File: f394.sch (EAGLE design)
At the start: 4 parts

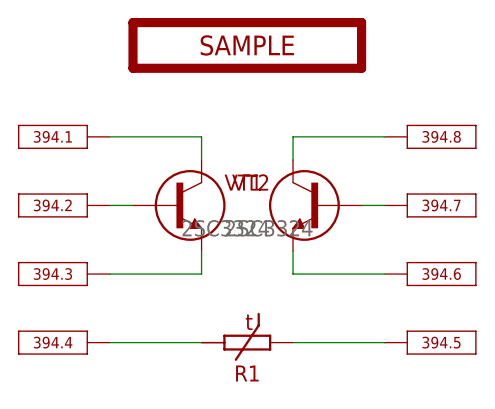
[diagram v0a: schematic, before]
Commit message: Update F394 to use PMP4201Y
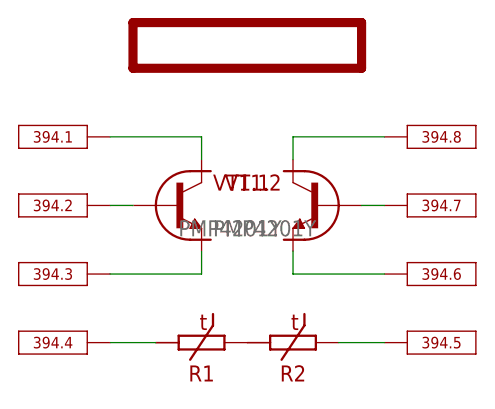
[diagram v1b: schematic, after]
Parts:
- removed VT2: 2SC3324, transistors-npn:2SC3324
- added R2: (no value), resistors:ERA-V33J102V
- 394: value SAMPLE -> (none)
- VT1: value 2SC3324 -> PMP4201Y; device transistors-npn:2SC3324 -> transistors-npn:PMP4201Y
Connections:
- removed net N$2: 394.2.PIN, VT1.B
- removed net N$5: 394.7.PIN, VT2.B
- removed net N$9 (its old number): 394.5.PIN, R1.E
- new net B1: 394.2.PIN, VT1.1.B
- new net B2: 394.7.PIN, VT1.2.B
- new net N$10: 394.5.PIN, R2.E
- new net N$7: R1.E, R2.A
- net N$1: now also VT1.1.C; no longer VT1.C
- net N$3: now also VT1.2.E; no longer VT2.E
- net N$4: now also VT1.2.C; no longer VT2.C
- net N$6: now also VT1.1.E; no longer VT1.E
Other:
- moved on the sheet: R1
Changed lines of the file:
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@@
 <?xml version="1.0" encoding="utf-8"?>
 <!DOCTYPE eagle SYSTEM "eagle.dtd">
-<eagle version="7.5.0">
+<eagle version="7.5.1">
 <drawing>
 <settings>
@@
 </classes>
 <parts>
-<part name="394" library="module-footprints" deviceset="DIP8" device="" value="SAMPLE"/>
-<part name="VT1" library="transistors-npn" deviceset="?" device="2SC3324"/>
-<part name="VT2" library="transistors-npn" deviceset="?" device="2SC3324"/>
+<part name="394" library="module-footprints" deviceset="DIP8" device=""/>
 <part name="R1" library="resistors" deviceset="ERA-?33J*V" device="V" technology="102"/>
+<part name="R2" library="resistors" deviceset="ERA-?33J*V" device="V" technology="102"/>
+<part name="VT1" library="transistors-npn" deviceset="PMP4201Y" device=""/>
 </parts>
 <sheets>
@@
 <instance part="394" gate=".5" x="76.2" y="50.8" rot="R180"/>
 <instance part="394" gate="G$1" x="58.42" y="83.82" rot="R180"/>
-<instance part="VT1" gate="G$1" x="50.8" y="66.04"/>
-<instance part="VT2" gate="G$1" x="66.04" y="66.04" rot="MR0"/>
-<instance part="R1" gate="G$1" x="58.42" y="50.8"/>
+<instance part="R1" gate="G$1" x="53.34" y="50.8"/>
+<instance part="R2" gate="G$1" x="63.5" y="50.8"/>
+<instance part="VT1" gate=".1" x="53.34" y="66.04"/>
+<instance part="VT1" gate=".2" x="63.5" y="66.04" rot="MR0"/>
 </instances>
 <busses>
@@
 <segment>
 <pinref part="394" gate=".1" pin="PIN"/>
-<pinref part="VT1" gate="G$1" pin="C"/>
 <wire x1="43.18" y1="73.66" x2="53.34" y2="73.66" width="0.1524" layer="91"/>
 <wire x1="53.34" y1="73.66" x2="53.34" y2="71.12" width="0.1524" layer="91"/>
-</segment>
-</net>
-<net name="N$2" class="0">
-<segment>
-<pinref part="VT1" gate="G$1" pin="B"/>
+<pinref part="VT1" gate=".1" pin="C"/>
+</segment>
+</net>
+<net name="B1" class="0">
+<segment>
 <pinref part="394" gate=".2" pin="PIN"/>
 <wire x1="45.72" y1="66.04" x2="43.18" y2="66.04" width="0.1524" layer="91"/>
+<pinref part="VT1" gate=".1" pin="B"/>
 </segment>
 </net>
@@
 <segment>
 <pinref part="394" gate=".6" pin="PIN"/>
-<pinref part="VT2" gate="G$1" pin="E"/>
 <wire x1="73.66" y1="58.42" x2="63.5" y2="58.42" width="0.1524" layer="91"/>
 <wire x1="63.5" y1="58.42" x2="63.5" y2="60.96" width="0.1524" layer="91"/>
+<pinref part="VT1" gate=".2" pin="E"/>
 </segment>
 </net>
@@
 <segment>
 <pinref part="394" gate=".8" pin="PIN"/>
-<pinref part="VT2" gate="G$1" pin="C"/>
 <wire x1="73.66" y1="73.66" x2="63.5" y2="73.66" width="0.1524" layer="91"/>
 <wire x1="63.5" y1="73.66" x2="63.5" y2="71.12" width="0.1524" layer="91"/>
-</segment>
-</net>
-<net name="N$5" class="0">
+<pinref part="VT1" gate=".2" pin="C"/>
+</segment>
+</net>
+<net name="B2" class="0">
 <segment>
 <pinref part="394" gate=".7" pin="PIN"/>
-<pinref part="VT2" gate="G$1" pin="B"/>
-<wire x1="73.66" y1="66.04" x2="71.12" y2="66.04" width="0.1524" layer="91"/>
-</segment>
-</net>
-<net name="N$9" class="0">
-<segment>
-<pinref part="R1" gate="G$1" pin="E"/>
-<pinref part="394" gate=".5" pin="PIN"/>
-<wire x1="63.5" y1="50.8" x2="73.66" y2="50.8" width="0.1524" layer="91"/>
+<pinref part="VT1" gate=".2" pin="B"/>
+<wire x1="71.12" y1="66.04" x2="73.66" y2="66.04" width="0.1524" layer="91"/>
 </segment>
 </net>
 <net name="N$6" class="0">
 <segment>
-<pinref part="VT1" gate="G$1" pin="E"/>
 <wire x1="53.34" y1="58.42" x2="53.34" y2="60.96" width="0.1524" layer="91"/>
 <pinref part="394" gate=".3" pin="PIN"/>
 <wire x1="43.18" y1="58.42" x2="53.34" y2="58.42" width="0.1524" layer="91"/>
+<pinref part="VT1" gate=".1" pin="E"/>
 </segment>
 </net>
 <net name="N$7" class="0">
+<segment>
+<pinref part="R1" gate="G$1" pin="E"/>
+<pinref part="R2" gate="G$1" pin="A"/>
+</segment>
+</net>
+<net name="N$9" class="0">
 <segment>
 <pinref part="394" gate=".4" pin="PIN"/>
 <pinref part="R1" gate="G$1" pin="A"/>
-<wire x1="43.18" y1="50.8" x2="53.34" y2="50.8" width="0.1524" layer="91"/>
-</segment>
-</net>
+<wire x1="43.18" y1="50.8" x2="48.26" y2="50.8" width="0.1524" layer="91"/>
+</segment>
+</net>
+<net name="N$10" class="0">
+<segment>
+<pinref part="R2" gate="G$1" pin="E"/>
+<pinref part="394" gate=".5" pin="PIN"/>
+<wire x1="68.58" y1="50.8" x2="73.66" y2="50.8" width="0.1524" layer="91"/>
+</segment>
+</net>
